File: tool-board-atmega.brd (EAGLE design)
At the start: 101.6 x 53.3 mm, 85 parts, among them IC3 ATMEGA2560-16AU, IC4 ATMEGA8U2-MU, Q1 16MHz, Q2 16MHz, X1 22-23-2031, X3 22-23-2031, X4 22-23-2031, X5 22-23-2021, X6 22-23-2021, X7 22-23-2021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

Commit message: board outline planned, some larger parts placed, schematic naming tweaks
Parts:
- removed X1, X3, X4: 22-23-2031, con-molex:22-23-2031
- removed X5, X6, X7, X8: 22-23-2021, con-molex:22-23-2021
- removed X9: 22-23-2101, con-molex:22-23-2101
- added DBG: 22-23-2101, con-molex:22-23-2101
- added SOL-12V, SOL-5V, STP-A, STP-B: 22-23-2021, con-molex:22-23-2021
- added SRV1, SRV2, SRV3: 22-23-2031, con-molex:22-23-2031
- moved U$18 299.2 mm to (-176.5, 48.3)
- moved RN8 297.3 mm to (-174.0, 43.2)
- moved U$21 296.7 mm to (-174.0, 48.3)
- moved U$20 296.5 mm to (-171.4, 48.3)
- moved U$19 296.3 mm to (-168.9, 48.3)
- moved RN7 292.0 mm to (-168.9, 43.2)
- moved U$17 285.7 mm to (-182.9, 47.0)
- moved U$16 282.6 mm to (-179.1, 47.0)
- moved U$14 271.9 mm to (-166.4, 48.3)
- moved L2 268.2 mm to (-143.5, 48.3)
- moved Z4 265.9 mm to (-158.8, 43.2)
- moved U$15 264.5 mm to (-147.3, 48.3)
- moved Z3 257.7 mm to (-148.6, 43.2)
- moved R12 256.1 mm to (-154.9, 30.5)
- moved R11 252.2 mm to (-160.0, 30.5)
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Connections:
- net +5V: now also DBG.2, SRV1.2, SRV2.2, SRV3.2; no longer X1.2, X3.2, X4.2, X9.2
- net GND: now also DBG.1, SRV1.1, SRV2.1, SRV3.1; no longer X1.1, X3.1, X4.1, X9.1
- net N$12: now also STP-B.2; no longer X5.2
- net N$13: now also STP-B.1; no longer X5.1
- net N$17: now also SOL-12V.2; no longer X7.2
- net N$18: now also SOL-5V.2; no longer X8.2
- net N$19: now also SOL-12V.1; no longer X7.1
- net N$20: now also DBG.10; no longer X9.10
- net N$21: now also SOL-5V.1; no longer X8.1
- net N$22: now also DBG.5; no longer X9.5
- net N$7: now also STP-A.1; no longer X6.1
- net N$8: now also STP-A.2; no longer X6.2
- net PE3: now also SRV1.3; no longer X1.3
- net PE4: now also SRV2.3; no longer X3.3
- net PE5: now also SRV3.3; no longer X4.3
- net PH3: now also DBG.6; no longer X9.6
- net PH4: now also DBG.7; no longer X9.7
- net PH5: now also DBG.8; no longer X9.8
- net PH6: now also DBG.9; no longer X9.9
- net RXD2: now also DBG.3; no longer X9.3
- net TXD2: now also DBG.4; no longer X9.4
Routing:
- net +5V: track 250.2 -> 0.00 mm, vias 23 -> 0
- net RESET: track 159.5 -> 0.00 mm, vias 6 -> 0
- net PB3: track 113.7 -> 0.00 mm, vias 3 -> 0
- net PB2: track 102.8 -> 0.00 mm, vias 3 -> 0
- net PB1: track 90.0 -> 0.00 mm, vias 3 -> 0
- net N$3: track 72.7 -> 0.00 mm, vias 4 -> 0
- net PB0: track 64.6 -> 0.00 mm, vias 2 -> 0
- net TXD2: track 56.0 -> 0.00 mm, vias 1 -> 0
- net RXD2: track 55.2 -> 0.00 mm, vias 1 -> 0
- net PE0: track 54.7 -> 0.00 mm, vias 2 -> 0
- net NSLEEP: track 53.6 -> 0.00 mm
- net PE1: track 52.5 -> 0.00 mm, vias 3 -> 0
- net DIR: track 52.3 -> 0.00 mm
- net GND: track 51.6 -> 0.00 mm, vias 47 -> 0
- net NSTEP: track 51.1 -> 0.00 mm
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- removed copper zone on layer 1, net +5V
- removed copper zone on layer 16, net +5V
- removed copper zone on layer 1, net GND
- removed copper zone on layer 16, net GND
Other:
- board size 101.6 x 53.3 mm -> 187.2 x 104 mm
- board text removed: "0"
- board text removed: "1"
- board text removed: "10"
- board text removed: "11"
- board text removed: "12"
- board text removed: "13"
- board text removed: "14"
- board text removed: "15"
- board text removed: "16"
- board text removed: "17"
- board text removed: "18"
- board text removed: "19"
- board text removed: "2"
- board text removed: "20"
- board text removed: "21"
- board text removed: "22"
- board text removed: "24"
- board text removed: "26"
- board text removed: "28"
- board text removed: "3"
- board text removed: "30"
- board text removed: "31"
- board text removed: "32"
- board text removed: "33"
- board text removed: "34"
- board text removed: "35"
- board text removed: "36"
- board text removed: "37"
- board text removed: "38"
- board text removed: "39"
- board text removed: "3V3"
- board text removed: "4"
- board text removed: "40"
- board text removed: "41"
- board text removed: "42"
- board text removed: "43"
- board text removed: "44"
- board text removed: "45"
- board text removed: "46"
- board text removed: "47"
- board text removed: "48"
- board text removed: "49"
- board text removed: "5"
- board text removed: "50"
- board text removed: "51"
- board text removed: "52"
- board text removed: "53"
- board text removed: "5V"
- board text removed: "6"
- board text removed: "7"
- board text removed: "8"
- board text removed: "9"
- board text removed: "ANALOG IN"
- board text removed: "AREF"
- board text removed: "Arduino"
- board text removed: "D.Cuartielles"
- board text removed: "D.Mellis"
- board text removed: "DIGITAL"
- board text removed: "G.Martino"
- board text removed: "GND"
- board text removed: "ITALY"
- board text removed: "L"
- board text removed: "M.Banzi"
- board text removed: "MADE IN"
- board text removed: "MEGA 2560"
- board text removed: "MEGAXL"
- board text removed: "PC1"
- board text removed: "PC2"
- board text removed: "PWM"
- board text removed: "RESET"
- board text removed: "RX"
- board text removed: "RX1"
- board text removed: "RX2"
- board text removed: "RX3"
- board text removed: "SCL"
- board text removed: "SDA"
- board text removed: "T.Igoe"
- board text removed: "TM"
- board text removed: "TX"
- board text removed: "TX1"
- board text removed: "TX2"
- board text removed: "TX3"
- board text removed: "VIN"
- board text removed: "designed by"
- board text removed: "tinker it"
- board text removed: "www.arduino.cc"

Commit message: schematic revision edits - thanks Jaden
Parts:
- removed R5: 27R, SmartPrj:R0603-ROUND
- added R13, R15: 1M, SmartPrj:R0603-ROUND
- added R14, R16: 100, SmartPrj:R0603-ROUND
- RN6: value 4k7 -> 2k2
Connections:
- new net N$2: R14.1, U$15.P$2
- new net N$36: R16.1, U$15.P$5
- net +5V: no longer RN6.5, RN6.6, RN6.7, RN6.8
- net GND: now also R13.2, R15.2, RN6.5, RN6.6, RN6.7, RN6.8
- net N$15: now also R15.1, R16.2; no longer U$15.P$5
- net N$16: now also R13.1, R14.2; no longer U$15.P$2

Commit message: library updates, changed diode package, added heat pad to DRV8825
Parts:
- U$1: device ClinicalRobotics:P-TSSOP28-1 -> ClinicalRobotics:DRV8825
- U$16, U$17: value DIODE_SOD323 -> DIODE0805; device ClinicalRobotics:SOD-323 -> ClinicalRobotics:0805LED
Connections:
- net GND: now also U$1.HEAT
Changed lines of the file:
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@@
 <attribute name="VALUE" x="-134.62" y="19.05" size="1.27" layer="27" rot="R90"/>
 </element>
-<element name="U$1" library="ClinicalRobotics" package="P-TSSOP28-1" value="DRV8825" x="-41.91" y="1.27" smashed="yes" rot="MR0">
+<element name="U$1" library="ClinicalRobotics" package="DRV8825" value="DRV8825" x="-41.91" y="1.27" smashed="yes" rot="MR0">
 <attribute name="NAME" x="-36.759" y="-1.3599" size="1.27" layer="26" rot="MR90"/>
 <attribute name="VALUE" x="-38.9851" y="0.59" size="1.27" layer="28" rot="MR0"/>
@@
 <element name="U$14" library="ClinicalRobotics" package="0805" value="4A" x="-166.37" y="48.26" smashed="yes"/>
 <element name="U$15" library="ClinicalRobotics" package="SC-88" value="DUALNMOS-SSM6N7002KFULFCT" x="-147.32" y="48.26" smashed="yes"/>
-<element name="U$16" library="ClinicalRobotics" package="SOD-323" value="DIODE_SOD323" x="-179.07" y="46.99" smashed="yes"/>
-<element name="U$17" library="ClinicalRobotics" package="SOD-323" value="DIODE_SOD323" x="-182.88" y="46.99" smashed="yes"/>
+<element name="U$16" library="ClinicalRobotics" package="0805LED" value="DIODE0805" x="-179.07" y="46.99" smashed="yes"/>
+<element name="U$17" library="ClinicalRobotics" package="0805LED" value="DIODE0805" x="-182.88" y="46.99" smashed="yes"/>
 <element name="U$18" library="ClinicalRobotics" package="RGBLED" value="RGBLED" x="-176.53" y="48.26" smashed="yes"/>
 <element name="U$19" library="ClinicalRobotics" package="0805LED" value="0805LED" x="-168.91" y="48.26" smashed="yes"/>
@@
 <contactref element="RN6" pad="7"/>
 <contactref element="RN6" pad="8"/>
+<contactref element="U$1" pad="HEAT"/>
 <wire x1="-184.531" y1="-55.88" x2="-184.531" y2="-68.58" width="0" layer="19" extent="1-1"/>
 <wire x1="-151.13" y1="21.37" x2="-184.531" y2="-55.88" width="0" layer="19" extent="1-1"/>
@@
 <wire x1="-33.91" y1="16.01" x2="-38.41" y2="24.51" width="0" layer="19" extent="1-1"/>
 <wire x1="-44.91" y1="8.51" x2="-49.91" y2="17.51" width="0" layer="19" extent="1-1"/>
-<wire x1="-37.685" y1="4.245" x2="-44.91" y2="8.51" width="0" layer="19" extent="1-16"/>
-<wire x1="-40.935" y1="-1.705" x2="-37.685" y2="4.245" width="0" layer="19" extent="16-16"/>
-<wire x1="-42.885" y1="-1.705" x2="-40.935" y2="-1.705" width="0" layer="19" extent="16-16"/>
+<wire x1="-41.91" y1="1.27" x2="-44.91" y2="8.51" width="0" layer="19" extent="1-16"/>
+<wire x1="-42.885" y1="-1.705" x2="-41.91" y2="1.27" width="0" layer="19" extent="16-16"/>
+<wire x1="-40.935" y1="-1.705" x2="-42.885" y2="-1.705" width="0" layer="19" extent="16-16"/>
 <wire x1="-46.135" y1="-1.705" x2="-42.885" y2="-1.705" width="0" layer="19" extent="16-16"/>
+<wire x1="-37.685" y1="4.245" x2="-41.91" y2="1.27" width="0" layer="19" extent="16-16"/>
 <wire x1="-54.61" y1="-8.89" x2="-46.135" y2="-1.705" width="0" layer="19" extent="1-16"/>
 <wire x1="-56.91" y1="-8.14" x2="-54.61" y2="-8.89" width="0" layer="19" extent="1-1"/>
@@
 <contactref element="SOL-12V" pad="2"/>
 <contactref element="U$16" pad="P$1"/>
-<wire x1="-180.125" y1="46.99" x2="-146.695" y2="47.135" width="0" layer="19" extent="1-1"/>
+<wire x1="-179.07" y1="47.9806" x2="-146.695" y2="47.135" width="0" layer="19" extent="1-1"/>
 <wire x1="24.501971875" y1="31.378025" x2="-146.695" y2="47.135" width="0" layer="19" extent="1-1"/>
 </signal>
@@
 <contactref element="SOL-5V" pad="2"/>
 <contactref element="U$17" pad="P$1"/>
-<wire x1="-183.935" y1="46.99" x2="-147.945" y2="49.135" width="0" layer="19" extent="1-1"/>
+<wire x1="-182.88" y1="47.9806" x2="-147.945" y2="49.135" width="0" layer="19" extent="1-1"/>
 <wire x1="35.56" y1="21.59" x2="-147.945" y2="49.135" width="0" layer="19" extent="1-1"/>
 </signal>
@@
 <contactref element="U$16" pad="P$2"/>
 <wire x1="-160.909" y1="30.48" x2="26.298025" y2="29.581971875" width="0" layer="19" extent="1-1"/>
-<wire x1="-178.015" y1="46.99" x2="-160.909" y2="30.48" width="0" layer="19" extent="1-1"/>
+<wire x1="-179.07" y1="45.9994" x2="-160.909" y2="30.48" width="0" layer="19" extent="1-1"/>
 </signal>
 <signal name="N$21">
@@
 <contactref element="R12" pad="1"/>
 <contactref element="U$17" pad="P$2"/>
-<wire x1="-181.825" y1="46.99" x2="-155.829" y2="30.48" width="0" layer="19" extent="1-1"/>
+<wire x1="-182.88" y1="45.9994" x2="-155.829" y2="30.48" width="0" layer="19" extent="1-1"/>
 <wire x1="35.56" y1="19.05" x2="-155.829" y2="30.48" width="0" layer="19" extent="1-1"/>
 </signal>

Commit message: riped up and started layout over, organized components into logical systems
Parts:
- removed U$14: 4A, ClinicalRobotics:0805
- added C19, C22: 100uF, rcl:E3,5-8
- added F2: 500mA, rcl:L1812
- C18: device SmartPrj:C0603-ROUND -> rcl:E3,5-8
- X2: value (none) -> MICROUSB_VERTICAL; device SmartPrj:PN61729 -> ClinicalRobotics:MICROUSB_VERT
- moved SOL-5V 233.6 mm to (-193.0, -27.9)
- moved SOL-12V 214.8 mm to (-170.2, -58.4)
- moved SRV3 203.7 mm to (-163.8, 53.3)
- moved SRV2 202.8 mm to (-162.6, 43.2)
- moved Z3 188.4 mm to (-43.2, -113.0)
- moved Z4 188.4 mm to (-53.3, -113.0)
- moved C8 176.1 mm to (-54.6, -95.2), flipped to the bottom
- moved STP-A 175.4 mm to (-139.7, -27.9), turned to 0 degrees
- moved STP-B 168.3 mm to (-132.1, -27.9), turned to 0 degrees
- moved RN3 165.9 mm to (-73.7, -105.4), turned to 90 degrees
- moved L2 165.2 mm to (-49.5, -87.6)
- moved RN2 162.7 mm to (-54.6, -87.6)
- moved GROUND 158.5 mm to (-48.3, -92.7)
- moved F1 155.9 mm to (-44.5, -97.8), turned to 270 degrees
- moved ON 150.1 mm to (-67.3, -104.1)
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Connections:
- removed net XVCC: F1.2, U$9.P$1, X2.1
- new net VCCPIN: F1.2, F2.2, U$9.P$1, X2.P$1
- net +12V: now also C19.+; no longer U$14.P$2
- net +12VIN: now also C18.+; no longer C18.1, U$14.P$1
- net +5V: now also C22.+, F2.1
- net D+: now also X2.P$3; no longer X2.3
- net D-: now also X2.P$2; no longer X2.2
- net DECAY: now also IC3.41; no longer IC3.36
- net DIR: now also IC3.40; no longer IC3.37
- net GND: now also C18.-, C19.-, C22.-; no longer C18.2
- net MODE0: now also IC3.37; no longer IC3.40
- net MODE1: now also IC3.36; no longer IC3.41
- net MODE2: now also IC3.35; no longer IC3.42
- net NENBL: now also IC3.39; no longer IC3.38
- net NSLEEP: now also IC3.42; no longer IC3.35
- net NSTEP: now also IC3.38; no longer IC3.39
- net UGND: now also X2.P$4; no longer X2.4
- net USHIELD: now also X2.P$6, X2.P$7; no longer X2.P$1, X2.P$2
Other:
- board size 187.2 x 104 mm -> 112 x 104 mm

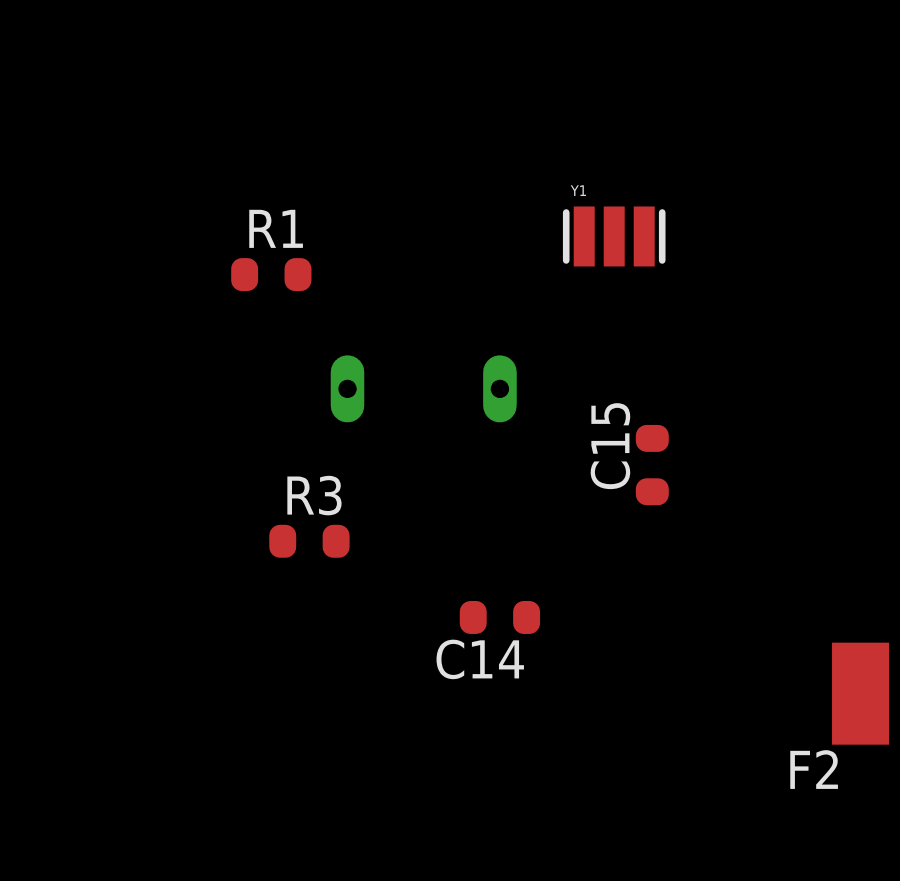
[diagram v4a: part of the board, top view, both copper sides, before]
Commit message: removed crystals from primary micro
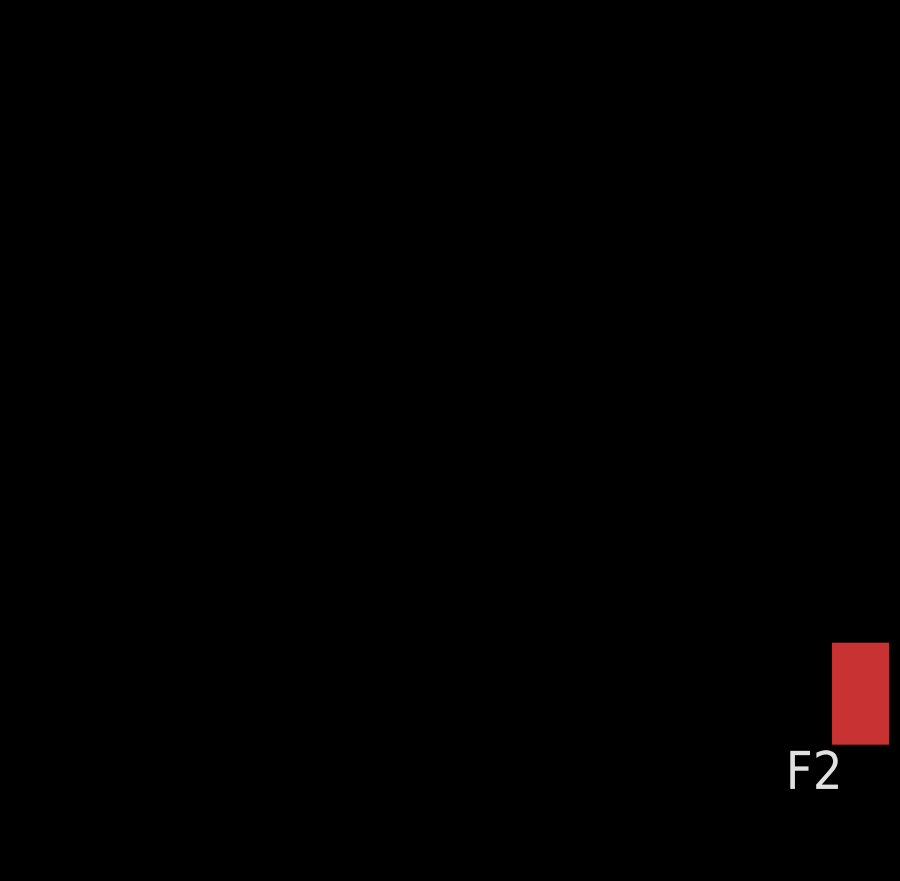
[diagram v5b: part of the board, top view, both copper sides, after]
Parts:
- removed C14, C15: 22p, SmartPrj:C0603-ROUND
- removed Q2: 16MHz, special:QS
- removed R1: 1M, SmartPrj:R0603-ROUND
- removed R3: 27R, SmartPrj:R0603-ROUND
- removed Y1: 16MHz, SmartPrj:RESONATOR
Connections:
- removed net XTAL1: C14.2, Q2.2, R1.1, R3.2, Y1.3
- removed net XTAL1R: IC3.34, R3.1
- removed net XTAL2: C15.2, IC3.33, Q2.1, R1.2, Y1.1
- net GND: no longer C14.1, C15.1, Y1.2
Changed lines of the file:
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@@
 <attribute name="VALUE" x="-118.999" y="-9.652" size="1.27" layer="27"/>
-</element>
-<element name="C14" library="SmartPrj" package="C0603-ROUND" value="22p" x="-44.45" y="52.07" smashed="yes" rot="R180">
-<attribute name="NAME" x="-43.561" y="51.308" size="1.27" layer="25" rot="R180"/>
-<attribute name="VALUE" x="-43.561" y="54.102" size="1.27" layer="27" rot="R180"/>
-</element>
-<element name="C15" library="SmartPrj" package="C0603-ROUND" value="22p" x="-39.37" y="57.15" smashed="yes" rot="R90">
-<attribute name="NAME" x="-40.132" y="56.261" size="1.27" layer="25" rot="R90"/>
-<attribute name="VALUE" x="-37.338" y="56.261" size="1.27" layer="27" rot="R90"/>
 </element>
 <element name="C16" library="SmartPrj" package="C0603-ROUND" value="22p" x="-101.6" y="-40.64" smashed="yes" rot="R90">
@@
 <attribute name="VALUE" x="-110.363" y="-41.91" size="1.27" layer="27" ratio="10" rot="R90"/>
 </element>
-<element name="Q2" library="special" package="QS" value="16MHz" x="-46.99" y="59.69" smashed="yes" rot="MR0">
-<attribute name="NAME" x="-41.91" y="62.357" size="1.27" layer="26" ratio="10" rot="MR0"/>
-<attribute name="VALUE" x="-41.91" y="55.753" size="1.27" layer="28" ratio="10" rot="MR0"/>
-</element>
-<element name="R1" library="SmartPrj" package="R0603-ROUND" value="1M" x="-52.07" y="63.5" smashed="yes">
-<attribute name="NAME" x="-52.959" y="64.389" size="1.27" layer="25"/>
-<attribute name="VALUE" x="-52.959" y="61.468" size="1.27" layer="27"/>
-</element>
 <element name="R10" library="SmartPrj" package="R0603-ROUND" value="4.7k" x="-139.7" y="-10.16" smashed="yes">
 <attribute name="NAME" x="-140.589" y="-9.271" size="1.27" layer="25"/>
@@
 <attribute name="NAME" x="-108.839" y="-35.941" size="1.27" layer="25"/>
 <attribute name="VALUE" x="-108.839" y="-38.862" size="1.27" layer="27"/>
-</element>
-<element name="R3" library="SmartPrj" package="R0603-ROUND" value="27R" x="-50.8" y="54.61" smashed="yes">
-<attribute name="NAME" x="-51.689" y="55.499" size="1.27" layer="25"/>
-<attribute name="VALUE" x="-51.689" y="52.578" size="1.27" layer="27"/>
 </element>
 <element name="R4" library="SmartPrj" package="R0603-ROUND" value="27R" x="-107.95" y="-43.18" smashed="yes">
@@
 <attribute name="OC_NEWARK" value="94C0765" x="-136.398" y="98.044" size="1.778" layer="27" rot="R180" display="off"/>
 <attribute name="VALUE" x="-97.028" y="76.454" size="1.016" layer="27" ratio="10" rot="R180"/>
-</element>
-<element name="Y1" library="SmartPrj" package="RESONATOR" value="16MHz" x="-40.64" y="64.77" smashed="yes">
-<attribute name="NAME" x="-42.09" y="66.12" size="0.3556" layer="25"/>
-<attribute name="VALUE" x="-42.09" y="63.082" size="0.3556" layer="27"/>
 </element>
 <element name="Y2" library="SmartPrj" package="RESONATOR" value="16MHz" x="-119.38" y="-48.26" smashed="yes">
@@
 <contactref element="UBOOT" pad="2"/>
 <contactref element="C8" pad="2"/>
-<contactref element="Y1" pad="2"/>
 <contactref element="C16" pad="2"/>
 <contactref element="C17" pad="2"/>
-<contactref element="C14" pad="1"/>
-<contactref element="C15" pad="1"/>
 <contactref element="SRV1" pad="1"/>
 <contactref element="SRV2" pad="1"/>
@@
 <wire x1="-79.61" y1="73.065" x2="-80.41" y2="73.065" width="0" layer="19" extent="1-1"/>
 <wire x1="-78.81" y1="73.065" x2="-79.61" y2="73.065" width="0" layer="19" extent="1-1"/>
-<wire x1="-40.64" y1="64.77" x2="-78.81" y2="73.065" width="0" layer="19" extent="1-1"/>
-<wire x1="-39.37" y1="56.261" x2="-40.64" y2="64.77" width="0" layer="19" extent="1-1"/>
-<wire x1="-43.561" y1="52.07" x2="-39.37" y2="56.261" width="0" layer="19" extent="1-1"/>
-<wire x1="-9.652" y1="45.72" x2="-39.37" y2="56.261" width="0" layer="19" extent="1-1"/>
-<wire x1="13.208" y1="45.72" x2="-9.652" y2="45.72" width="0" layer="19" extent="1-1"/>
 <wire x1="-165.1" y1="29.21" x2="-138.811" y2="-10.16" width="0" layer="19" extent="1-1"/>
 <wire x1="-162.56" y1="40.64" x2="-165.1" y2="29.21" width="0" layer="19" extent="1-1"/>
@@
 <wire x1="-47.498" y1="-92.71" x2="-55.46" y2="-95.25" width="0" layer="19" extent="1-16"/>
 <wire x1="-67.31" y1="-103.09" x2="-55.46" y2="-95.25" width="0" layer="19" extent="1-16"/>
+<wire x1="-9.652" y1="45.72" x2="-74.55" y2="23.63" width="0" layer="19" extent="1-1"/>
+<wire x1="13.208" y1="45.72" x2="-9.652" y2="45.72" width="0" layer="19" extent="1-1"/>
 </signal>
 <signal name="AREF">
@@
 <wire x1="0" y1="48.895" x2="-50.63" y2="-87.63" width="0" layer="19" extent="1-1"/>
 </signal>
-<signal name="XTAL2">
-<contactref element="IC3" pad="33"/>
-<contactref element="Y1" pad="1"/>
-<contactref element="R1" pad="2"/>
-<contactref element="Q2" pad="1"/>
-<contactref element="C15" pad="2"/>
-<wire x1="-51.181" y1="63.5" x2="-85.05" y2="16.13" width="0" layer="19" extent="1-1"/>
-<wire x1="-44.45" y1="59.69" x2="-51.181" y2="63.5" width="0" layer="19" extent="1-1"/>
-<wire x1="-39.37" y1="58.039" x2="-44.45" y2="59.69" width="0" layer="19" extent="1-1"/>
-<wire x1="-41.64" y1="64.77" x2="-44.45" y2="59.69" width="0" layer="19" extent="1-1"/>
-</signal>
-<signal name="XTAL1">
-<contactref element="Q2" pad="2"/>
-<contactref element="C14" pad="2"/>
-<contactref element="R1" pad="1"/>
-<contactref element="Y1" pad="3"/>
-<contactref element="R3" pad="2"/>
-<wire x1="-49.53" y1="59.69" x2="-39.64" y2="64.77" width="0" layer="19" extent="1-1"/>
-<wire x1="-49.911" y1="54.61" x2="-49.53" y2="59.69" width="0" layer="19" extent="1-1"/>
-<wire x1="-52.959" y1="63.5" x2="-49.53" y2="59.69" width="0" layer="19" extent="1-1"/>
-<wire x1="-45.339" y1="52.07" x2="-49.911" y2="54.61" width="0" layer="19" extent="1-1"/>
-</signal>
 <signal name="XT2">
 <contactref element="Y2" pad="1"/>
@@
 <wire x1="-114.3" y1="-34.29" x2="-108.839" y2="-36.83" width="0" layer="19" extent="1-1"/>
 </signal>
-<signal name="XTAL1R">
-<contactref element="IC3" pad="34"/>
-<contactref element="R3" pad="1"/>
-<wire x1="-51.689" y1="54.61" x2="-84.55" y2="16.13" width="0" layer="19" extent="1-1"/>
-</signal>
 <signal name="XT1R">
